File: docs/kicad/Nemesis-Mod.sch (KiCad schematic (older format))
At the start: 16 parts, among them M1 Pololu G2 HighPower 18v17, M1-M1 Pololu G2 HighPower 18v18, P1 Power, SW1 Reset, SW2 Rev SPDT Trigger, SW3 Firing SPDT Trigger

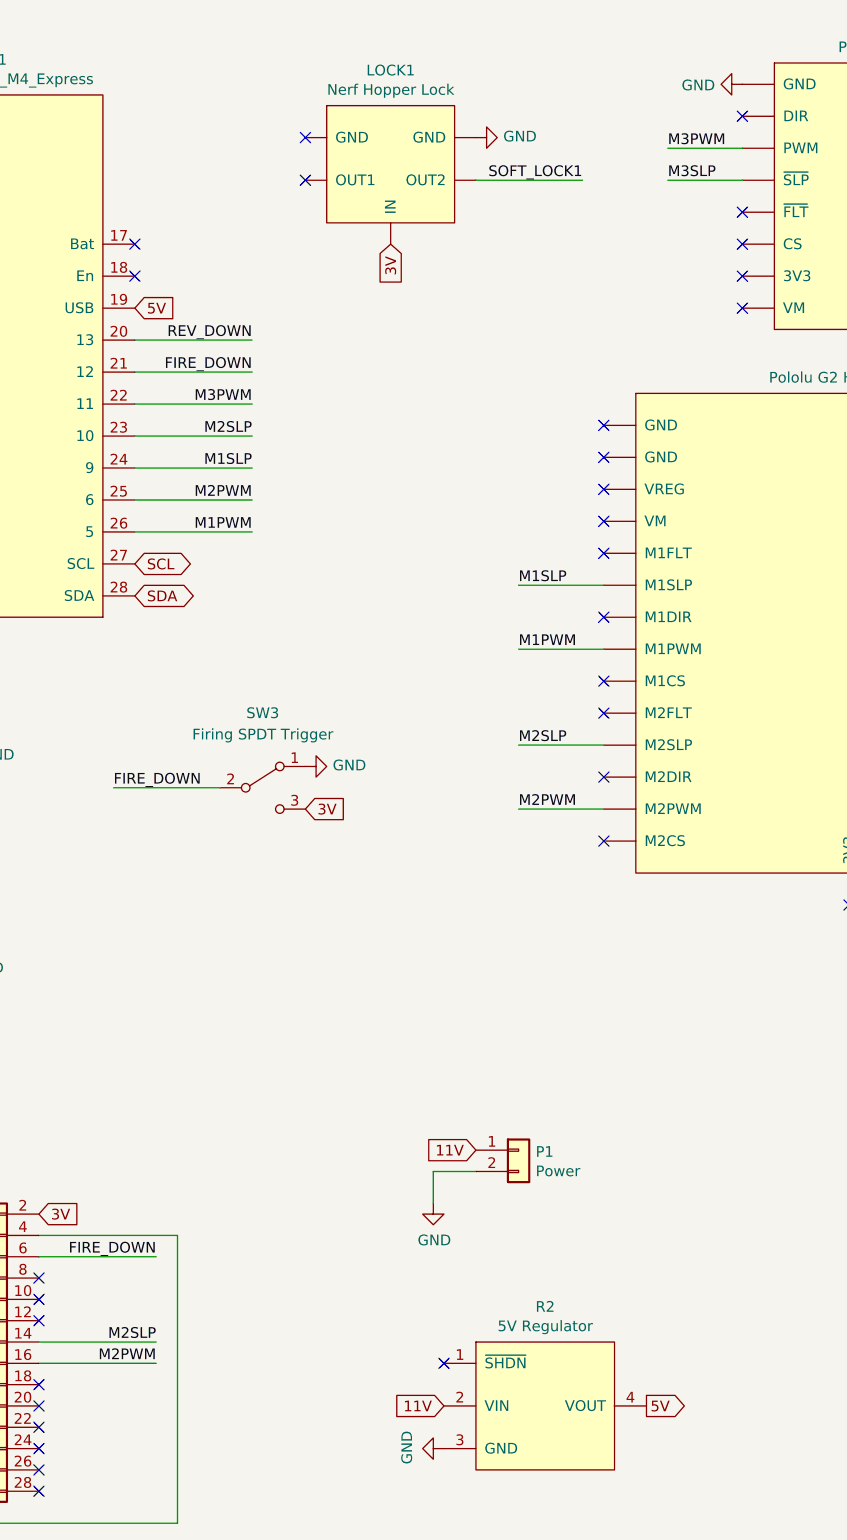
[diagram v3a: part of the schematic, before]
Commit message: Fixing schematic issues after double checking before fabrication.
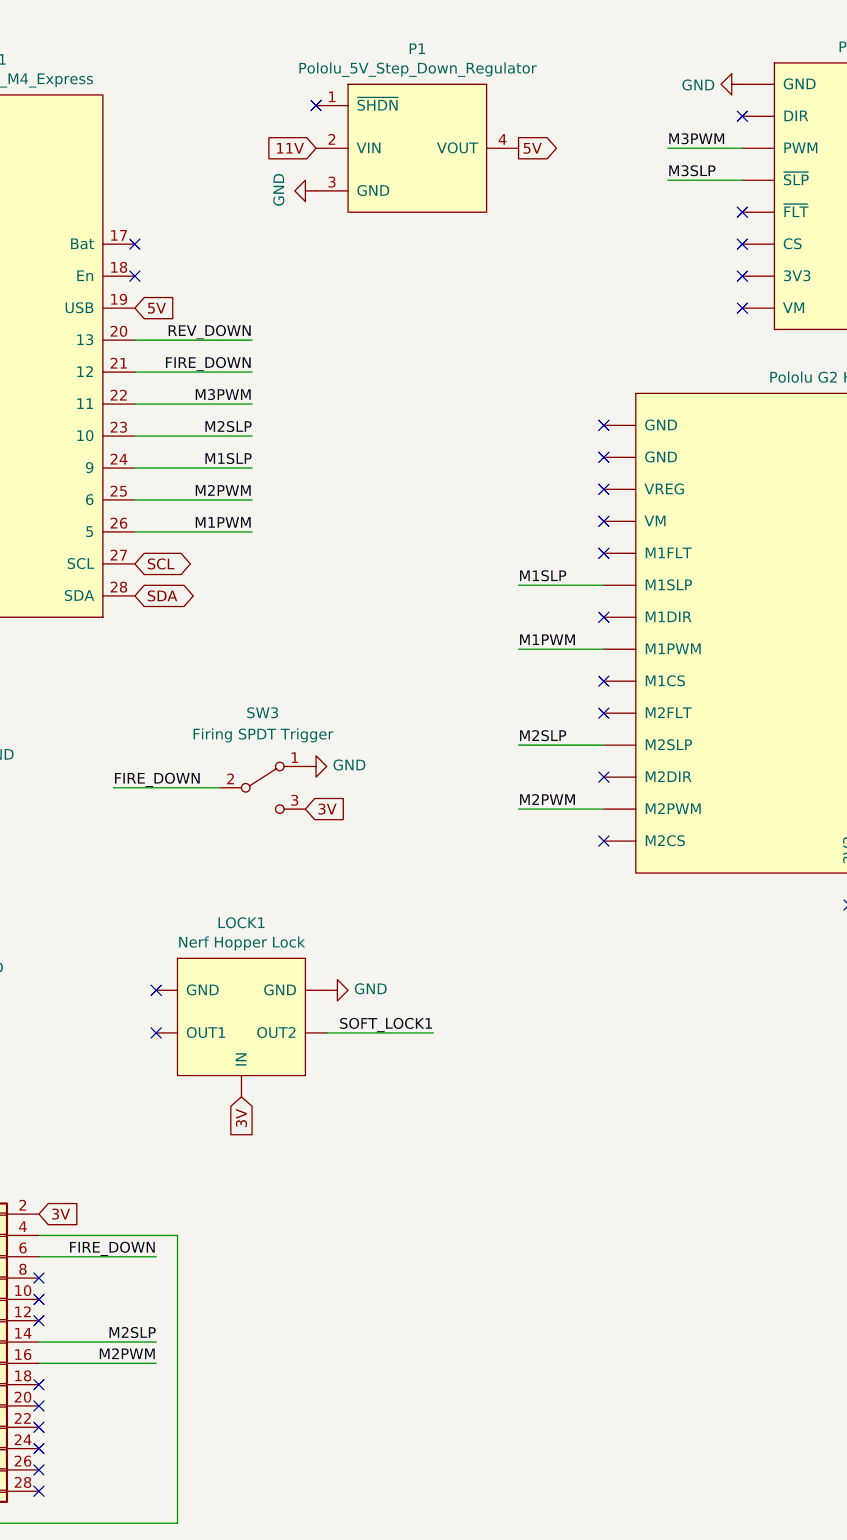
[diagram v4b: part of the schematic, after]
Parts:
- removed P1: Power, Connector_PinHeader_2.54mm:PinHeader_1x02_P2.54mm_Vertical, symbol Connector_Generic:Conn_01x02
- removed R2: 5V Regulator, Connector_PinHeader_2.54mm:PinHeader_1x04_P2.54mm_Vertical, symbol Nemesis-Mod:Pololu_5V_Step_Down_Regulator
- added P1: Pololu_5V_Step_Down_Regulator, Pololu:5V_Step_Down_Regulator_500mA, symbol Nemesis-Mod:Pololu_5V_Step_Down_Regulator
- F1: footprint Connector_PinHeader_2.54mm:PinHeader_1x08_P2.54mm_Vertical -> Adafruit:Adafruit_I2C_FRAM_Breakout
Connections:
- net 11V: now also P1.2 (VIN)
- net 5V: now also P1.4 (VOUT)
- net GND: now also P1.3 (GND)
- new net: BATT1.1 (+), M1-M1.~ (VREG), M1.~ (~SLP)
- new net: BATT1.2 (-), M1-M1.~ (VREG), M1.~ (~SLP)
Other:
- moved on the sheet: LOCK1
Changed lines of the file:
@@
 Text GLabel 2700 3150 2    50   BiDi ~ 0
 SCL
-Text GLabel 3900 1650 3    50   Input ~ 0
-3V
-NoConn ~ 3500 1150
-NoConn ~ 3500 1350
+Text GLabel 3200 5650 3    50   Input ~ 0
+3V
+NoConn ~ 2800 5150
+NoConn ~ 2800 5350
 Text Label 850  2250 0    50   ~ 0
 RESET_DOWN
@@
 L Nemesis-Mod:Nerf_Hopper_Lock LOCK1
 U 1 1 5F60175A
-P 3900 1250
-F 0 "LOCK1" H 3900 1665 50  0000 C CNN
-F 1 "Nerf Hopper Lock" H 3900 1574 50  0000 C CNN
-F 2 "" H 3900 1550 50  0001 C CNN
-F 3 "" H 3900 1550 50  0001 C CNN
-	1    3900 1250
-	1    0    0    -1
-$EndComp
-Text Label 4800 1350 2    50   ~ 0
+P 3200 5250
+F 0 "LOCK1" H 3200 5665 50  0000 C CNN
+F 1 "Nerf Hopper Lock" H 3200 5574 50  0000 C CNN
+F 2 "" H 3200 5550 50  0001 C CNN
+F 3 "" H 3200 5550 50  0001 C CNN
+	1    3200 5250
+	1    0    0    -1
+$EndComp
+Text Label 4100 5350 2    50   ~ 0
 SOFT_LOCK1
 Wire Wire Line
-	4300 1350 4800 1350
+	3600 5350 4100 5350
 Text Label 850  2400 0    50   ~ 0
 SOFT_LOCK1
@@
 NoConn ~ 5550 1950
 NoConn ~ 5550 1050
-Text GLabel 5100 7100 2    50   Output ~ 0
+Text GLabel 4500 1200 2    50   Output ~ 0
 5V
 Text Notes 9650 3750 2    50   ~ 0
@@
 Text GLabel 6650 4750 3    50   Output ~ 0
 11V
-Text GLabel 4150 7100 0    50   Input ~ 0
+Text GLabel 3550 1200 0    50   Input ~ 0
 11V
 NoConn ~ 6350 4750
@@
 L power:GND #PWR07
 U 1 1 61B28A20
-P 4150 7300
-F 0 "#PWR07" H 4150 7050 50  0001 C CNN
-F 1 "GND" H 4155 7127 50  0000 C CNN
-F 2 "" H 4150 7300 50  0001 C CNN
-F 3 "" H 4150 7300 50  0001 C CNN
-	1    4150 7300
+P 3550 1400
+F 0 "#PWR07" H 3550 1150 50  0001 C CNN
+F 1 "GND" H 3555 1227 50  0000 C CNN
+F 2 "" H 3550 1400 50  0001 C CNN
+F 3 "" H 3550 1400 50  0001 C CNN
+	1    3550 1400
 	0    1    -1   0
 $EndComp
@@
 L power:GND #PWR08
 U 1 1 61B45500
-P 4300 1150
-F 0 "#PWR08" H 4300 900 50  0001 C CNN
-F 1 "GND" V 4305 1022 50  0000 R CNN
-F 2 "" H 4300 1150 50  0001 C CNN
-F 3 "" H 4300 1150 50  0001 C CNN
-	1    4300 1150
+P 3600 5150
+F 0 "#PWR08" H 3600 4900 50  0001 C CNN
+F 1 "GND" V 3605 5022 50  0000 R CNN
+F 2 "" H 3600 5150 50  0001 C CNN
+F 3 "" H 3600 5150 50  0001 C CNN
+	1    3600 5150
 	0    -1   -1   0
 $EndComp
@@
 Text Label 2800 6800 2    50   ~ 0
 M2SLP
-$Comp
-L Connector_Generic:Conn_01x02 P1
-U 1 1 61BD9B06
-P 4500 5900
-F 0 "P1" H 4580 5892 50  0000 L CNN
-F 1 "Power" H 4580 5801 50  0000 L CNN
-F 2 "Connector_PinHeader_2.54mm:PinHeader_1x02_P2.54mm_Vertical" H 4500 5900 50  0001 C CNN
-F 3 "https://www.adafruit.com/product/724" H 4500 5900 50  0001 C CNN
-F 4 "724" H 4500 5900 50  0001 C CNN "MPN"
-	1    4500 5900
-	1    0    0    -1
-$EndComp
-Text GLabel 4300 5900 0    50   Input ~ 0
-11V
-Wire Wire Line
-	4300 6000 4100 6000
-Wire Wire Line
-	4100 6000 4100 6150
-$Comp
-L power:GND #PWR06
-U 1 1 61BDDD6B
-P 4100 6150
-F 0 "#PWR06" H 4100 5900 50  0001 C CNN
-F 1 "GND" H 4105 5977 50  0000 C CNN
-F 2 "" H 4100 6150 50  0001 C CNN
-F 3 "" H 4100 6150 50  0001 C CNN
-	1    4100 6150
-	1    0    0    -1
-$EndComp
 Wire Wire Line
 	1750 7300 1250 7300
@@
 $EndComp
 $Comp
-L Nemesis-Mod:Pololu_5V_Step_Down_Regulator R2
-U 1 1 61C57817
-P 4800 7650
-F 0 "R2" H 4625 8665 50  0000 C CNN
-F 1 "5V Regulator" H 4625 8574 50  0000 C CNN
-F 2 "Connector_PinHeader_2.54mm:PinHeader_1x04_P2.54mm_Vertical" H 4650 7700 50  0001 C CNN
-F 3 "" H 4650 7700 50  0001 C CNN
-	1    4800 7650
-	1    0    0    -1
-$EndComp
-NoConn ~ 4150 6900
-$Comp
 L Nemesis-Mod:Adafruit_I2C_FRAM_Breakout F1
 U 1 1 61C6969C
@@
 F 0 "F1" V 8950 5650 50  0000 C CNN
 F 1 "FRAM Breakout" V 8850 5650 50  0000 C CNN
-F 2 "Connector_PinHeader_2.54mm:PinHeader_1x08_P2.54mm_Vertical" H 8100 6200 50  0001 C CNN
+F 2 "Adafruit:Adafruit_I2C_FRAM_Breakout" H 8100 6200 50  0001 C CNN
 F 3 "" H 8100 6200 50  0001 C CNN
 	1    8250 5750
 	0    -1   -1   0
 $EndComp
+$Comp
+L Nemesis-Mod:Pololu_5V_Step_Down_Regulator P1
+U 1 1 61B01FC1
+P 4200 1750
+F 0 "P1" H 4025 2765 50  0000 C CNN
+F 1 "Pololu_5V_Step_Down_Regulator" H 4025 2674 50  0000 C CNN
+F 2 "Pololu:5V_Step_Down_Regulator_500mA" H 4050 1800 50  0001 C CNN
+F 3 "" H 4050 1800 50  0001 C CNN
+	1    4200 1750
+	1    0    0    -1
+$EndComp
+NoConn ~ 3550 1000
 $EndSCHEMATC
